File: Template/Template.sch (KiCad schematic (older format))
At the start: 1 part, among them J1 Bus_ISA_8bit

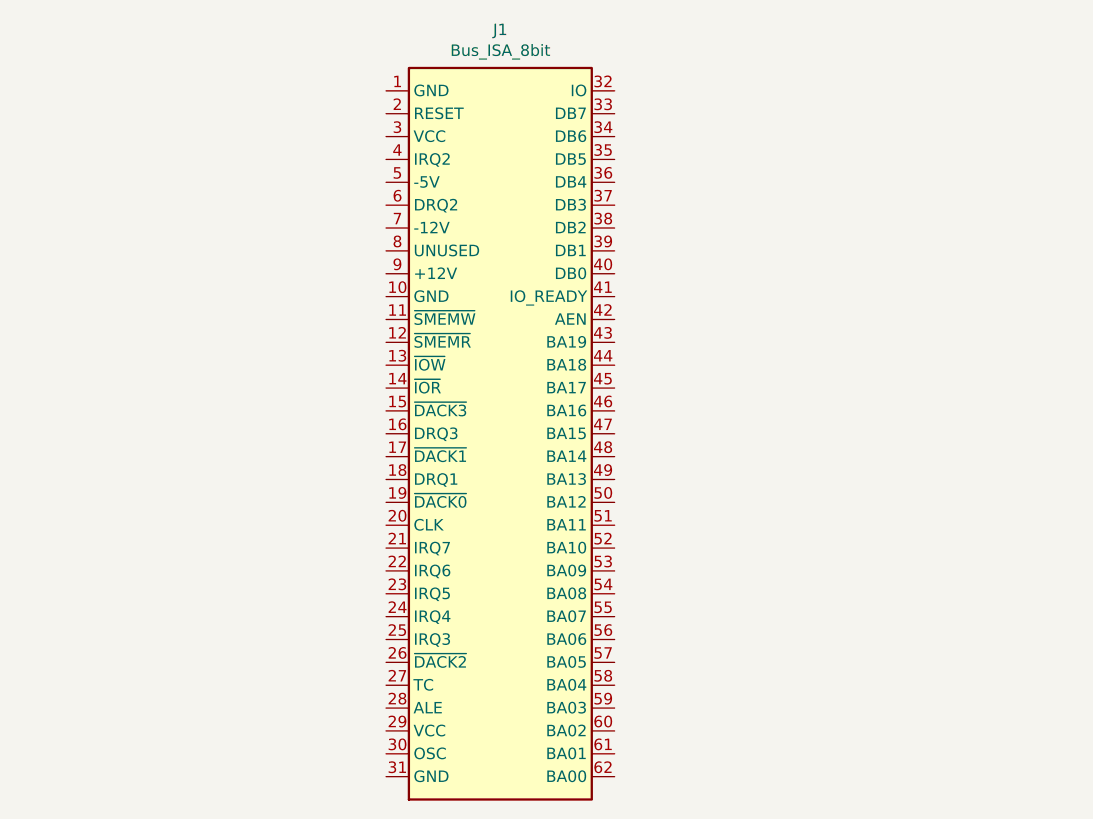
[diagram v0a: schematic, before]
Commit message: Add IDE/ATA connector to Template.
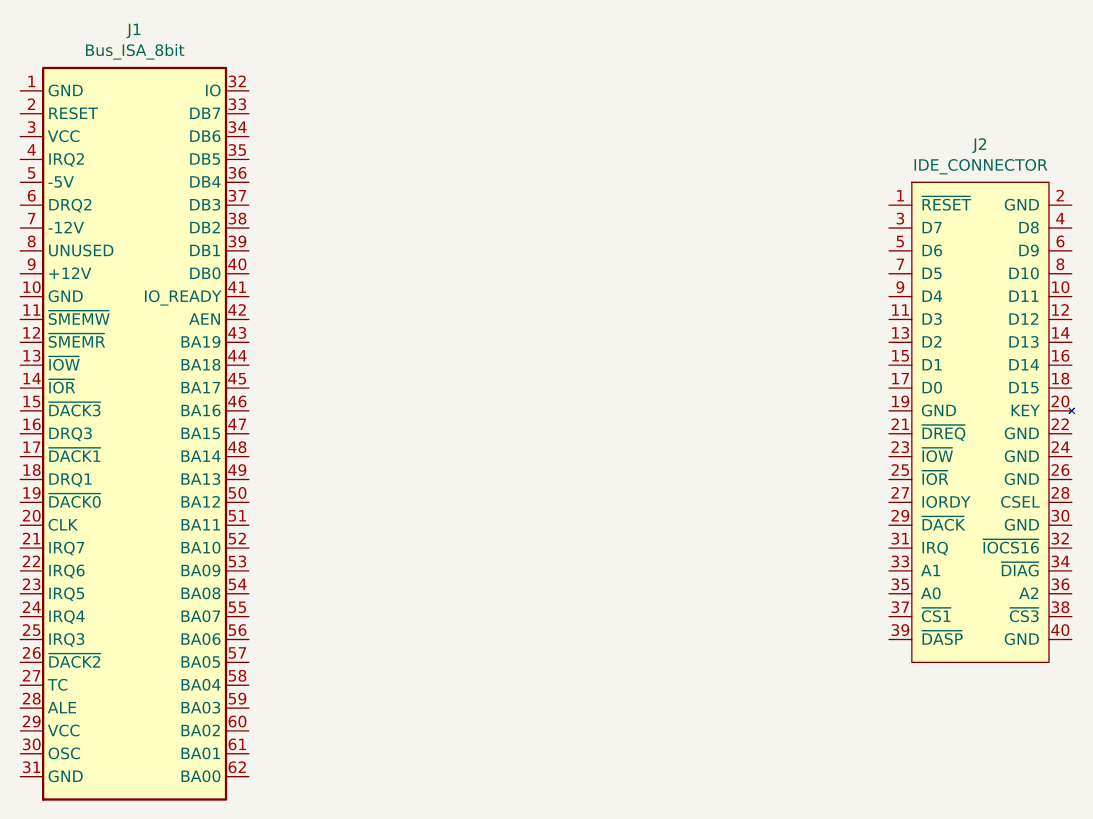
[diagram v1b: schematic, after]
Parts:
- added J2: IDE_CONNECTOR, Connector_PinSocket_2.54mm:PinSocket_2x20_P2.54mm_Vertical, symbol 00Common:IDE_CONNECTOR
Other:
- moved on the sheet: J1
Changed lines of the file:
@@
 L 00Common:Bus_ISA_8bit J1
 U 1 1 6039F90B
-P 5650 3750
-F 0 "J1" H 5650 5517 50  0000 C CNN
-F 1 "Bus_ISA_8bit" H 5650 5426 50  0000 C CNN
-F 2 "00Custom:BUS_XT" H 5650 3750 50  0001 C CNN
-F 3 "https://en.wikipedia.org/wiki/Industry_Standard_Architecture" H 5650 3750 50  0001 C CNN
-	1    5650 3750
+P 4050 3750
+F 0 "J1" H 4050 5517 50  0000 C CNN
+F 1 "Bus_ISA_8bit" H 4050 5426 50  0000 C CNN
+F 2 "00Custom:BUS_XT" H 4050 3750 50  0001 C CNN
+F 3 "https://en.wikipedia.org/wiki/Industry_Standard_Architecture" H 4050 3750 50  0001 C CNN
+	1    4050 3750
 	1    0    0    -1
 $EndComp
+$Comp
+L 00Common:IDE_CONNECTOR J2
+U 1 1 603ACBF3
+P 7750 2650
+F 0 "J2" H 7750 2815 50  0000 C CNN
+F 1 "IDE_CONNECTOR" H 7750 2724 50  0000 C CNN
+F 2 "Connector_PinSocket_2.54mm:PinSocket_2x20_P2.54mm_Vertical" H 7750 2650 50  0001 C CNN
+F 3 "" H 7750 2650 50  0001 C CNN
+	1    7750 2650
+	1    0    0    -1
+$EndComp

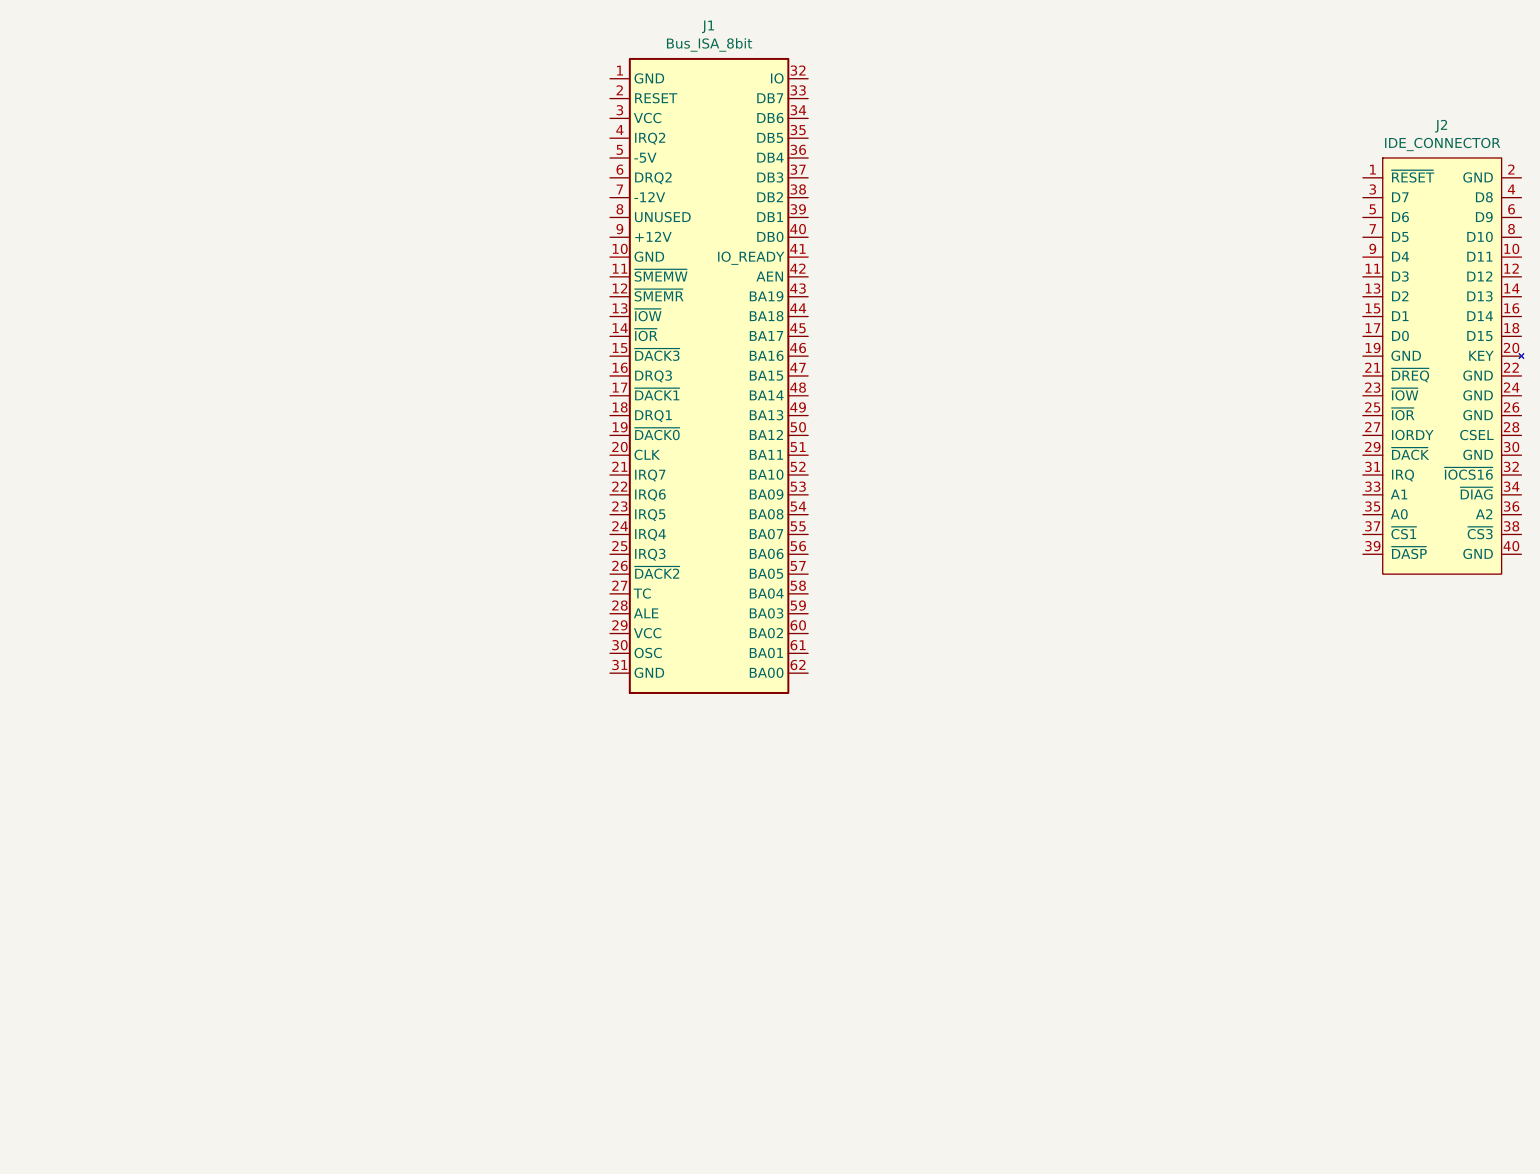
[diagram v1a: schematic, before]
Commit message: Add global labels to the ISA bus connector,
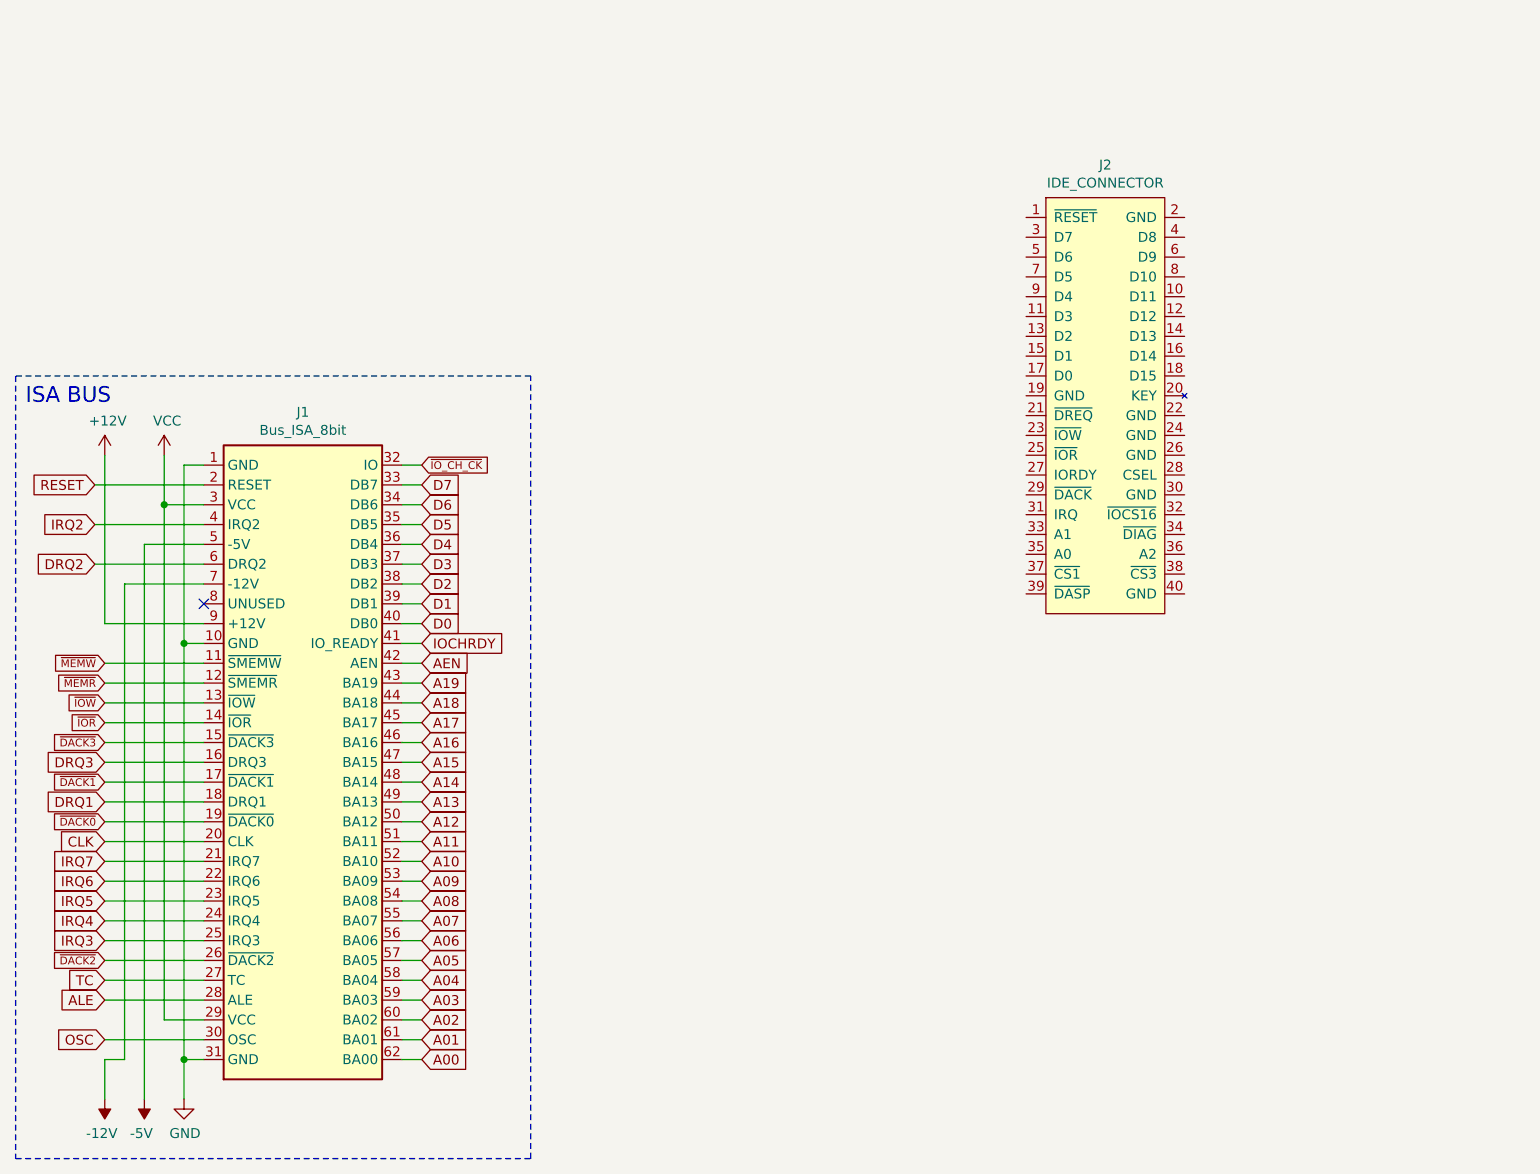
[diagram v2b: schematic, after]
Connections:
- net GND: now reaches J1.1 (GND)
- net GND: now also J1.10 (GND), J1.31 (GND)
- net ~MEMW: now reaches J1.11 (~SMEMW)
- net ~MEMR: now reaches J1.12 (~SMEMR)
- net ~IOW: now reaches J1.13 (~IOW)
- net ~IOR: now reaches J1.14 (~IOR)
- net ~DACK3: now reaches J1.15 (~DACK3)
- net DRQ3: now reaches J1.16 (DRQ3)
- net ~DACK1: now reaches J1.17 (~DACK1)
- net DRQ1: now reaches J1.18 (DRQ1)
- net ~DACK0: now reaches J1.19 (~DACK0)
- net RESET: now reaches J1.2 (RESET)
- net CLK: now reaches J1.20 (CLK)
- net IRQ7: now reaches J1.21 (IRQ7)
- net IRQ6: now reaches J1.22 (IRQ6)
- net IRQ5: now reaches J1.23 (IRQ5)
- net IRQ4: now reaches J1.24 (IRQ4)
- net IRQ3: now reaches J1.25 (IRQ3)
- net ~DACK2: now reaches J1.26 (~DACK2)
- net TC: now reaches J1.27 (TC)
- net ALE: now reaches J1.28 (ALE)
- net VCC: now reaches J1.29 (VCC)
- net VCC: now also J1.3 (VCC)
- net OSC: now reaches J1.30 (OSC)
- net ~IO_CH_CK: now reaches J1.32 (IO)
- net D7: now reaches J1.33 (DB7)
- net D6: now reaches J1.34 (DB6)
- net D5: now reaches J1.35 (DB5)
- net D4: now reaches J1.36 (DB4)
- net D3: now reaches J1.37 (DB3)
- net D2: now reaches J1.38 (DB2)
- net D1: now reaches J1.39 (DB1)
- net IRQ2: now reaches J1.4 (IRQ2)
- net D0: now reaches J1.40 (DB0)
- net IOCHRDY: now reaches J1.41 (IO_READY)
- net AEN: now reaches J1.42 (AEN)
- net A19: now reaches J1.43 (BA19)
- net A18: now reaches J1.44 (BA18)
- net A17: now reaches J1.45 (BA17)
- net A16: now reaches J1.46 (BA16)
- net A15: now reaches J1.47 (BA15)
- net A14: now reaches J1.48 (BA14)
- net A13: now reaches J1.49 (BA13)
- net -5V: now reaches J1.5 (-5V)
- net A12: now reaches J1.50 (BA12)
- net A11: now reaches J1.51 (BA11)
- net A10: now reaches J1.52 (BA10)
- net A09: now reaches J1.53 (BA09)
- net A08: now reaches J1.54 (BA08)
- net A07: now reaches J1.55 (BA07)
- net A06: now reaches J1.56 (BA06)
- net A05: now reaches J1.57 (BA05)
- net A04: now reaches J1.58 (BA04)
- net A03: now reaches J1.59 (BA03)
- net DRQ2: now reaches J1.6 (DRQ2)
- net A02: now reaches J1.60 (BA02)
- net A01: now reaches J1.61 (BA01)
- net A00: now reaches J1.62 (BA00)
- net -12V: now reaches J1.7 (-12V)
- net +12V: now reaches J1.9 (+12V)
- no-connect marks 0 -> 1
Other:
- note added: "ISA BUS"
- moved on the sheet: J1

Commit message: Add power for CF adapter to Template and CF-Super-Lite.
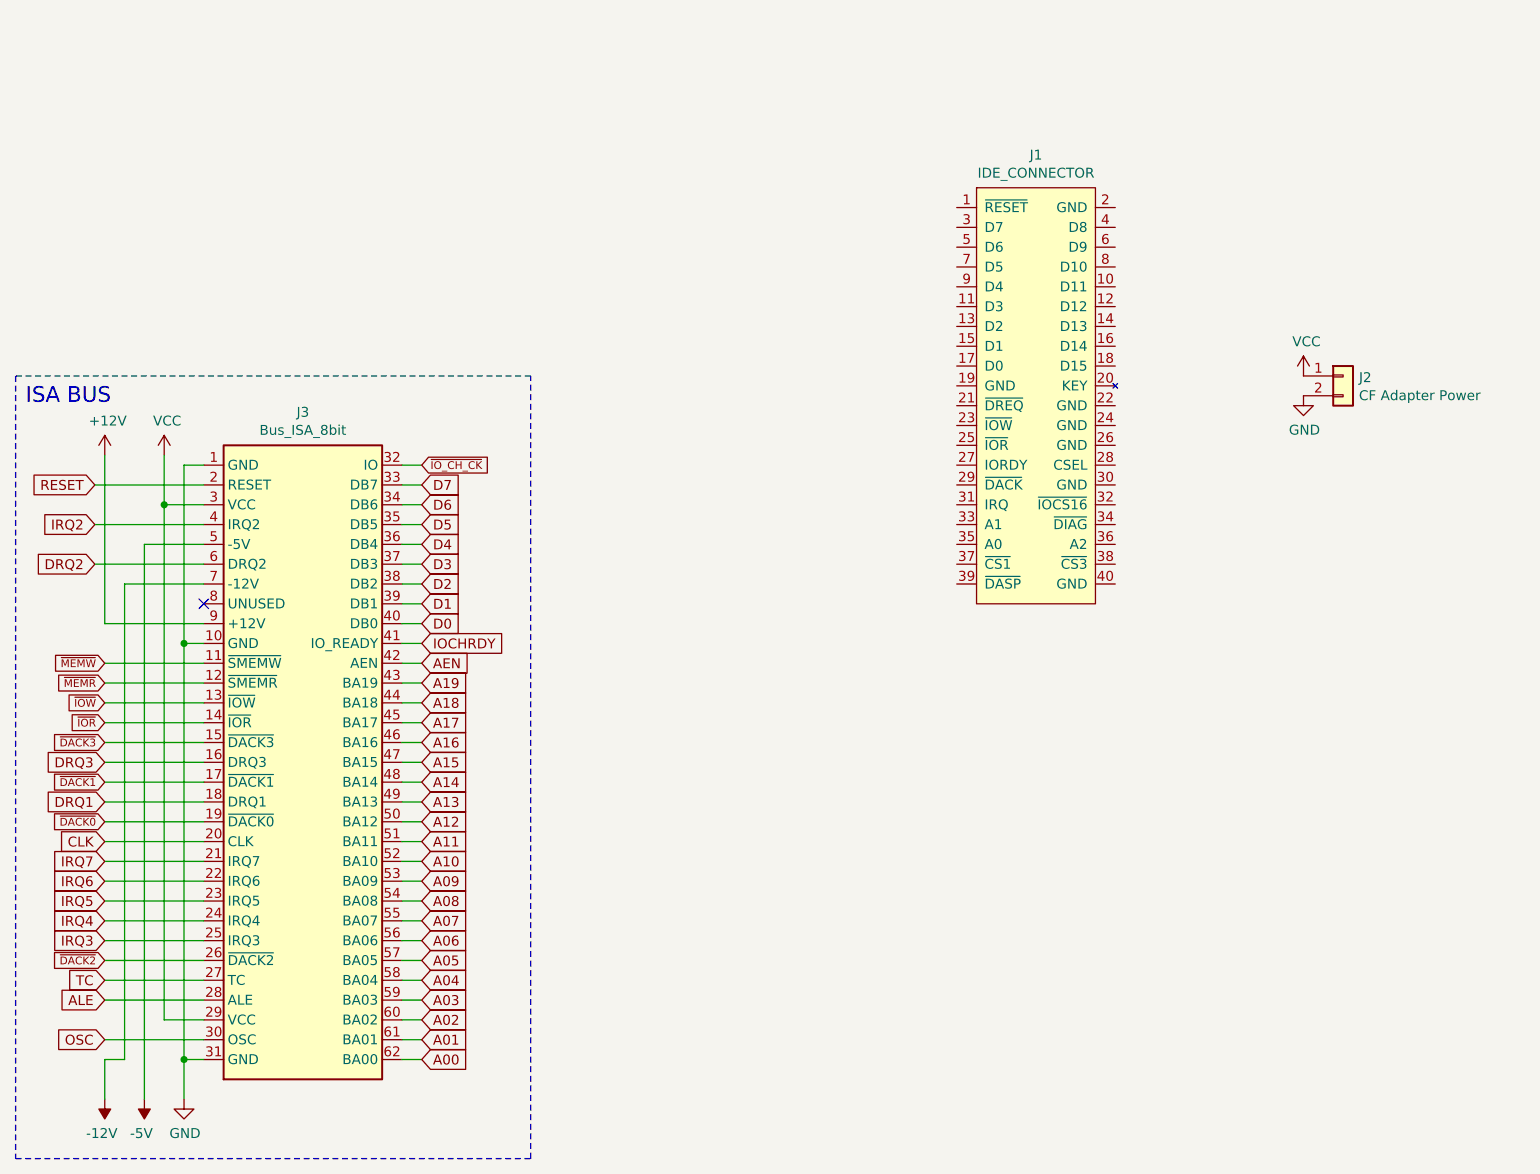
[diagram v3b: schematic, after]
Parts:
- removed J2: IDE_CONNECTOR, Connector_PinSocket_2.54mm:PinSocket_2x20_P2.54mm_Vertical, symbol 00Common:IDE_CONNECTOR
- added J1: IDE_CONNECTOR, Connector_PinSocket_2.54mm:PinSocket_2x20_P2.54mm_Vertical, symbol 00Common:IDE_CONNECTOR
- added J2: CF Adapter Power, Connector_PinHeader_2.54mm:PinHeader_1x02_P2.54mm_Vertical, symbol Connector_Generic:Conn_01x02
- renumbered J1 to J3
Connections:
- net GND: now also J2.2 (Pin_2)
- net VCC: now also J2.1 (Pin_1)
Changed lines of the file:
@@
 	1500 6900 1000 6900
 $Comp
-L 00Common:Bus_ISA_8bit J1
+L 00Common:Bus_ISA_8bit J3
 U 1 1 6039F90B
 P 2000 5700
-F 0 "J1" H 2000 7467 50  0000 C CNN
+F 0 "J3" H 2000 7467 50  0000 C CNN
 F 1 "Bus_ISA_8bit" H 2000 7376 50  0000 C CNN
 F 2 "00Custom:BUS_XT" H 2000 5700 50  0001 C CNN
@@
 	950  4500 1500 4500
 $Comp
-L 00Common:IDE_CONNECTOR J2
-U 1 1 60482C53
-P 6050 2850
-F 0 "J2" H 6050 3015 50  0000 C CNN
-F 1 "IDE_CONNECTOR" H 6050 2924 50  0000 C CNN
-F 2 "Connector_PinSocket_2.54mm:PinSocket_2x20_P2.54mm_Vertical" H 6050 2850 50  0001 C CNN
-F 3 "" H 6050 2850 50  0001 C CNN
-	1    6050 2850
+L 00Common:IDE_CONNECTOR J1
+U 1 1 603E88FA
+P 5700 2800
+F 0 "J1" H 5700 2965 50  0000 C CNN
+F 1 "IDE_CONNECTOR" H 5700 2874 50  0000 C CNN
+F 2 "Connector_PinSocket_2.54mm:PinSocket_2x20_P2.54mm_Vertical" H 5700 2800 50  0001 C CNN
+F 3 "" H 5700 2800 50  0001 C CNN
+	1    5700 2800
 	1    0    0    -1
 $EndComp
+$Comp
+L Connector_Generic:Conn_01x02 J2
+U 1 1 603ED503
+P 7250 3750
+F 0 "J2" H 7330 3742 50  0000 L CNN
+F 1 "CF Adapter Power" H 7330 3651 50  0000 L CNN
+F 2 "Connector_PinHeader_2.54mm:PinHeader_1x02_P2.54mm_Vertical" H 7250 3750 50  0001 C CNN
+F 3 "~" H 7250 3750 50  0001 C CNN
+	1    7250 3750
+	1    0    0    -1
+$EndComp
+$Comp
+L power:VCC #PWR0106
+U 1 1 603EE1D0
+P 7050 3750
+F 0 "#PWR0106" H 7050 3600 50  0001 C CNN
+F 1 "VCC" H 7065 3923 50  0000 C CNN
+F 2 "" H 7050 3750 50  0001 C CNN
+F 3 "" H 7050 3750 50  0001 C CNN
+	1    7050 3750
+	1    0    0    -1
+$EndComp
+$Comp
+L power:GND #PWR0107
+U 1 1 603EF04F
+P 7050 3850
+F 0 "#PWR0107" H 7050 3600 50  0001 C CNN
+F 1 "GND" H 7055 3677 50  0000 C CNN
+F 2 "" H 7050 3850 50  0001 C CNN
+F 3 "" H 7050 3850 50  0001 C CNN
+	1    7050 3850
+	1    0    0    -1
+$EndComp
